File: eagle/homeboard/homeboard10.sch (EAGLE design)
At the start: 99 parts, among them IC1 XCF02S, IC2 25LC080SN, IC3 ATMEGA32U2-TQFP, Q5 BC848SMD, Q6 BC848SMD, Q7 BC848SMD, Q8 BC848SMD, T1 BSS138, T2 BC848, T3 BSS138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

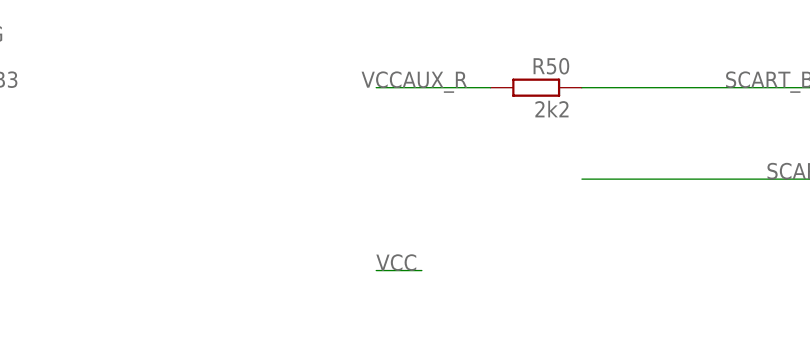
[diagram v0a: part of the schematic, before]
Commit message: reconnecting blanking pin
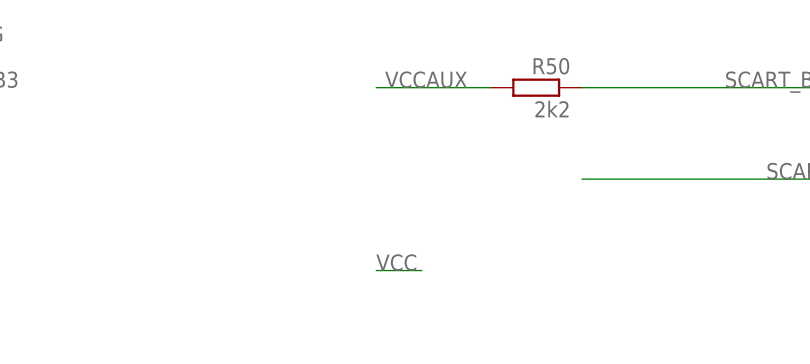
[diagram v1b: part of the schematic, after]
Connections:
- removed net VCCAUX_R: R50.2
- net VCCAUX: now also R50.2
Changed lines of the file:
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@@
 <junction x="-144.78" y="-73.66"/>
+</segment>
+<segment>
+<pinref part="R50" gate="G$1" pin="2"/>
+<wire x1="205.74" y1="276.86" x2="193.04" y2="276.86" width="0.1524" layer="91"/>
+<label x="203.2" y="276.86" size="1.778" layer="95" rot="MR0"/>
 </segment>
 </net>
@@
 </segment>
 </net>
-<net name="VCCAUX_R" class="0">
-<segment>
-<pinref part="R50" gate="G$1" pin="2"/>
-<wire x1="205.74" y1="276.86" x2="193.04" y2="276.86" width="0.1524" layer="91"/>
-<label x="203.2" y="276.86" size="1.778" layer="95" rot="MR0"/>
-</segment>
-</net>

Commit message: rework
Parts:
- added R47, R51: 270, rcl:R-EU_R0805
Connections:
- net CLK_5V: now also R47.1
- net DATA_5V: now also R51.1
- net PS2CLK: now also R47.2
- net PS2DAT: now also R51.2
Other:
- note added: "Possible alternative:"
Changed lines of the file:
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@@
 <part name="SUPPLY10" library="supply2" deviceset="GND" device=""/>
 <part name="SUPPLY11" library="supply2" deviceset="GND" device=""/>
+<part name="R47" library="rcl" deviceset="R-EU_" device="R0805" value="270"/>
+<part name="R51" library="rcl" deviceset="R-EU_" device="R0805" value="270"/>
 </parts>
 <sheets>
@@
 <plain>
 <text x="-167.64" y="86.36" size="1.778" layer="91">Choose one of these 3.3v regs</text>
+<text x="271.78" y="-254" size="1.778" layer="91">Possible alternative:</text>
 </plain>
 <instances>
@@
 <instance part="SUPPLY10" gate="GND" x="-149.86" y="50.8"/>
 <instance part="SUPPLY11" gate="GND" x="-149.86" y="27.94"/>
+<instance part="R47" gate="G$1" x="254" y="-261.62" rot="R180"/>
+<instance part="R51" gate="G$1" x="307.34" y="-261.62" rot="R180"/>
 </instances>
 <busses>
@@
 <label x="224.536" y="-196.342" size="1.778" layer="95"/>
 </segment>
+<segment>
+<wire x1="236.22" y1="-261.62" x2="248.92" y2="-261.62" width="0.1524" layer="91"/>
+<junction x="236.22" y="-261.62"/>
+<label x="232.156" y="-264.922" size="1.778" layer="95"/>
+<pinref part="R47" gate="G$1" pin="2"/>
+</segment>
 </net>
 <net name="PS2DAT" class="0">
@@
 <label x="286.004" y="-196.088" size="1.778" layer="95"/>
 </segment>
+<segment>
+<wire x1="292.1" y1="-261.62" x2="302.26" y2="-261.62" width="0.1524" layer="91"/>
+<junction x="292.1" y="-261.62"/>
+<label x="286.004" y="-264.668" size="1.778" layer="95"/>
+<pinref part="R51" gate="G$1" pin="2"/>
+</segment>
 </net>
 <net name="DATA_5V" class="0">
@@
 <label x="309.88" y="-228.6" size="1.778" layer="95"/>
 </segment>
+<segment>
+<junction x="332.74" y="-261.62"/>
+<label x="331.724" y="-264.922" size="1.778" layer="95"/>
+<pinref part="R51" gate="G$1" pin="1"/>
+<wire x1="312.42" y1="-261.62" x2="332.74" y2="-261.62" width="0.1524" layer="91"/>
+</segment>
 </net>
 <net name="CLK_5V" class="0">
@@
 <label x="309.88" y="-220.98" size="1.778" layer="95"/>
 </segment>
-</net>
+<segment>
+<wire x1="259.08" y1="-261.62" x2="269.24" y2="-261.62" width="0.1524" layer="91"/>
+<junction x="269.24" y="-261.62"/>
+<label x="268.478" y="-264.668" size="1.778" layer="95"/>
+<pinref part="R47" gate="G$1" pin="1"/>
+</segment>
+</net>

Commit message: rework
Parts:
- added C26, C27, C28, C29, C30, C31, C32: 100nF, rcl:C-EUC0603
- added R53, R54: 22, rcl:R-EU_R0805
- added X6: MINI-USB_4P-85-32004-10X, con-cypressindustries:MINI-USB_4P-85-32004-10X
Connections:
- new net N$36: R53.1, X6.2
- new net N$49: IC3.D+, R54.2
- new net N$66: R54.1, X6.3
- new net N$68: IC3.D-, R53.2
- new net N$69: IC3.UGND, X6.4
- net GND: now also C26.2, C27.2, C28.2, C29.2, C30.2, C31.2, C32.2, IC3.GND
- net VCC: now also C26.1, C27.1, C28.1, C29.1, C30.1, C31.1, C32.1, IC3.AVCC, IC3.UVCC, IC3.VCC
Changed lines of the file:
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@@
 <part name="R47" library="rcl" deviceset="R-EU_" device="R0805" value="270"/>
 <part name="R51" library="rcl" deviceset="R-EU_" device="R0805" value="270"/>
+<part name="C26" library="rcl" deviceset="C-EU" device="C0603" value="100nF"/>
+<part name="C27" library="rcl" deviceset="C-EU" device="C0603" value="100nF"/>
+<part name="C28" library="rcl" deviceset="C-EU" device="C0603" value="100nF"/>
+<part name="C29" library="rcl" deviceset="C-EU" device="C0603" value="100nF"/>
+<part name="C30" library="rcl" deviceset="C-EU" device="C0603" value="100nF"/>
+<part name="C31" library="rcl" deviceset="C-EU" device="C0603" value="100nF"/>
+<part name="C32" library="rcl" deviceset="C-EU" device="C0603" value="100nF"/>
+<part name="X6" library="con-cypressindustries" deviceset="MINI-USB_4P-" device="85-32004-10X"/>
+<part name="R53" library="rcl" deviceset="R-EU_" device="R0805" value="22"/>
+<part name="R54" library="rcl" deviceset="R-EU_" device="R0805" value="22"/>
+<part name="SUPPLY12" library="supply2" deviceset="GND" device=""/>
 </parts>
 <sheets>
@@
 <instance part="R47" gate="G$1" x="254" y="-261.62" rot="R180"/>
 <instance part="R51" gate="G$1" x="307.34" y="-261.62" rot="R180"/>
+<instance part="C26" gate="G$1" x="-147.32" y="127"/>
+<instance part="C27" gate="G$1" x="-139.7" y="127"/>
+<instance part="C28" gate="G$1" x="-132.08" y="127"/>
+<instance part="C29" gate="G$1" x="-101.6" y="127"/>
+<instance part="C30" gate="G$1" x="-124.46" y="127"/>
+<instance part="C31" gate="G$1" x="-116.84" y="127"/>
+<instance part="C32" gate="G$1" x="-109.22" y="127"/>
+<instance part="X6" gate="G$1" x="-299.72" y="-35.56" rot="MR0"/>
+<instance part="R53" gate="G$1" x="-281.94" y="-33.02" rot="MR180"/>
+<instance part="R54" gate="G$1" x="-287.02" y="-35.56" rot="MR180"/>
+<instance part="SUPPLY12" gate="GND" x="-292.1" y="-78.74"/>
 </instances>
 <busses>
@@
 <wire x1="-71.12" y1="104.14" x2="-63.5" y2="104.14" width="0.1524" layer="91"/>
 <junction x="-71.12" y="104.14"/>
+<pinref part="C26" gate="G$1" pin="2"/>
+<wire x1="-157.48" y1="121.92" x2="-147.32" y2="121.92" width="0.1524" layer="91"/>
+<pinref part="C27" gate="G$1" pin="2"/>
+<wire x1="-147.32" y1="121.92" x2="-139.7" y2="121.92" width="0.1524" layer="91"/>
+<junction x="-147.32" y="121.92"/>
+<pinref part="C28" gate="G$1" pin="2"/>
+<wire x1="-139.7" y1="121.92" x2="-132.08" y2="121.92" width="0.1524" layer="91"/>
+<junction x="-139.7" y="121.92"/>
+<pinref part="C30" gate="G$1" pin="2"/>
+<wire x1="-132.08" y1="121.92" x2="-124.46" y2="121.92" width="0.1524" layer="91"/>
+<junction x="-132.08" y="121.92"/>
+<pinref part="C31" gate="G$1" pin="2"/>
+<wire x1="-124.46" y1="121.92" x2="-116.84" y2="121.92" width="0.1524" layer="91"/>
+<junction x="-124.46" y="121.92"/>
+<pinref part="C32" gate="G$1" pin="2"/>
+<wire x1="-116.84" y1="121.92" x2="-109.22" y2="121.92" width="0.1524" layer="91"/>
+<junction x="-116.84" y="121.92"/>
+<pinref part="C29" gate="G$1" pin="2"/>
+<wire x1="-109.22" y1="121.92" x2="-101.6" y2="121.92" width="0.1524" layer="91"/>
+<junction x="-109.22" y="121.92"/>
+<wire x1="-157.48" y1="121.92" x2="-157.48" y2="104.14" width="0.1524" layer="91"/>
+<junction x="-157.48" y="104.14"/>
 </segment>
 <segment>
@@
 <junction x="-127" y="30.48"/>
 <pinref part="SUPPLY11" gate="GND" pin="GND"/>
+</segment>
+<segment>
+<pinref part="IC3" gate="G$1" pin="GND"/>
+<pinref part="SUPPLY12" gate="GND" pin="GND"/>
+<wire x1="-292.1" y1="-76.2" x2="-292.1" y2="-73.66" width="0.1524" layer="91"/>
+<wire x1="-292.1" y1="-73.66" x2="-274.32" y2="-73.66" width="0.1524" layer="91"/>
 </segment>
 </net>
@@
 </segment>
 <segment>
+<pinref part="C26" gate="G$1" pin="1"/>
+<pinref part="C27" gate="G$1" pin="1"/>
+<wire x1="-147.32" y1="129.54" x2="-139.7" y2="129.54" width="0.1524" layer="91"/>
+<junction x="-147.32" y="129.54"/>
+<pinref part="C28" gate="G$1" pin="1"/>
+<wire x1="-139.7" y1="129.54" x2="-132.08" y2="129.54" width="0.1524" layer="91"/>
+<junction x="-139.7" y="129.54"/>
+<pinref part="C30" gate="G$1" pin="1"/>
+<wire x1="-132.08" y1="129.54" x2="-124.46" y2="129.54" width="0.1524" layer="91"/>
+<junction x="-132.08" y="129.54"/>
+<pinref part="C31" gate="G$1" pin="1"/>
+<wire x1="-124.46" y1="129.54" x2="-116.84" y2="129.54" width="0.1524" layer="91"/>
+<junction x="-124.46" y="129.54"/>
+<pinref part="C32" gate="G$1" pin="1"/>
+<wire x1="-116.84" y1="129.54" x2="-109.22" y2="129.54" width="0.1524" layer="91"/>
+<junction x="-116.84" y="129.54"/>
+<pinref part="C29" gate="G$1" pin="1"/>
+<wire x1="-109.22" y1="129.54" x2="-101.6" y2="129.54" width="0.1524" layer="91"/>
+<junction x="-109.22" y="129.54"/>
 <wire x1="-167.64" y1="91.44" x2="-170.18" y2="91.44" width="0.1524" layer="91"/>
 <label x="-167.64" y="91.44" size="1.778" layer="95"/>
@@
 <wire x1="-172.72" y1="91.44" x2="-170.18" y2="91.44" width="0.1524" layer="91"/>
 <pinref part="C6" gate="G$1" pin="1"/>
-<wire x1="-170.18" y1="111.76" x2="-147.32" y2="111.76" width="0.1524" layer="91"/>
+<wire x1="-170.18" y1="111.76" x2="-165.1" y2="111.76" width="0.1524" layer="91"/>
 <junction x="-170.18" y="111.76"/>
 <pinref part="C7" gate="G$1" pin="1"/>
+<wire x1="-165.1" y1="111.76" x2="-147.32" y2="111.76" width="0.1524" layer="91"/>
 <wire x1="-147.32" y1="111.76" x2="-139.7" y2="111.76" width="0.1524" layer="91"/>
 <junction x="-147.32" y="111.76"/>
@@
 <wire x1="-71.12" y1="111.76" x2="-63.5" y2="111.76" width="0.1524" layer="91"/>
 <junction x="-71.12" y="111.76"/>
+<wire x1="-147.32" y1="129.54" x2="-165.1" y2="129.54" width="0.1524" layer="91"/>
+<wire x1="-165.1" y1="129.54" x2="-165.1" y2="111.76" width="0.1524" layer="91"/>
+<junction x="-165.1" y="111.76"/>
+</segment>
+<segment>
+<pinref part="IC3" gate="G$1" pin="AVCC"/>
+<wire x1="-274.32" y1="-25.4" x2="-279.4" y2="-25.4" width="0.1524" layer="91"/>
+<pinref part="IC3" gate="G$1" pin="UVCC"/>
+<wire x1="-274.32" y1="-22.86" x2="-279.4" y2="-22.86" width="0.1524" layer="91"/>
+<wire x1="-279.4" y1="-22.86" x2="-279.4" y2="-25.4" width="0.1524" layer="91"/>
+<junction x="-279.4" y="-25.4"/>
+<pinref part="IC3" gate="G$1" pin="VCC"/>
+<wire x1="-274.32" y1="-20.32" x2="-279.4" y2="-20.32" width="0.1524" layer="91"/>
+<wire x1="-279.4" y1="-20.32" x2="-279.4" y2="-22.86" width="0.1524" layer="91"/>
+<junction x="-279.4" y="-22.86"/>
+<wire x1="-279.4" y1="-25.4" x2="-289.56" y2="-25.4" width="0.1524" layer="91"/>
+<label x="-289.56" y="-25.4" size="1.778" layer="95"/>
 </segment>
 </net>
@@
 </segment>
 </net>
+<net name="N$36" class="0">
+<segment>
+<pinref part="X6" gate="G$1" pin="2"/>
+<wire x1="-294.64" y1="-33.02" x2="-287.02" y2="-33.02" width="0.1524" layer="91"/>
+<pinref part="R53" gate="G$1" pin="1"/>
+</segment>
+</net>
+<net name="N$66" class="0">
+<segment>
+<pinref part="R54" gate="G$1" pin="1"/>
+<pinref part="X6" gate="G$1" pin="3"/>
+<wire x1="-292.1" y1="-35.56" x2="-294.64" y2="-35.56" width="0.1524" layer="91"/>
+</segment>
+</net>
+<net name="N$68" class="0">
+<segment>
+<pinref part="IC3" gate="G$1" pin="D-"/>
+<wire x1="-276.86" y1="-33.02" x2="-274.32" y2="-33.02" width="0.1524" layer="91"/>
+<pinref part="R53" gate="G$1" pin="2"/>
+</segment>
+</net>
+<net name="N$49" class="0">
+<segment>
+<pinref part="IC3" gate="G$1" pin="D+"/>
+<wire x1="-274.32" y1="-35.56" x2="-281.94" y2="-35.56" width="0.1524" layer="91"/>
+<pinref part="R54" gate="G$1" pin="2"/>
+</segment>
+</net>
+<net name="N$69" class="0">
+<segment>
+<pinref part="X6" gate="G$1" pin="4"/>
+<wire x1="-294.64" y1="-38.1" x2="-292.1" y2="-38.1" width="0.1524" layer="91"/>
+<wire x1="-292.1" y1="-38.1" x2="-292.1" y2="-71.12" width="0.1524" layer="91"/>
+<pinref part="IC3" gate="G$1" pin="UGND"/>
+<wire x1="-292.1" y1="-71.12" x2="-274.32" y2="-71.12" width="0.1524" layer="91"/>
+</segment>
+</net>

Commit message: power socket
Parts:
- added X8: DC21MMX, powersupply:DC21MMX
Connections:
- net GND: now also X8.1, X8.3
- net VCC5: now also X8.2
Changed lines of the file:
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@@
 <clearance class="1" value="0.4"/>
+</class>
+<class number="2" name="gnd" width="0.3048" drill="0.508">
+<clearance class="2" value="0.1524"/>
 </class>
 </classes>
@@
 <part name="R54" library="rcl" deviceset="R-EU_" device="R0805" value="22"/>
 <part name="SUPPLY12" library="supply2" deviceset="GND" device=""/>
+<part name="X8" library="powersupply" deviceset="DC21MM" device="X"/>
+<part name="SUPPLY13" library="supply2" deviceset="GND" device=""/>
 </parts>
 <sheets>
@@
 <instance part="R54" gate="G$1" x="-287.02" y="-35.56" rot="MR180"/>
 <instance part="SUPPLY12" gate="GND" x="-292.1" y="-78.74"/>
+<instance part="X8" gate="G$1" x="-256.54" y="106.68"/>
+<instance part="SUPPLY13" gate="GND" x="-261.62" y="83.82"/>
 </instances>
 <busses>
@@
 <wire x1="-292.1" y1="-76.2" x2="-292.1" y2="-73.66" width="0.1524" layer="91"/>
 <wire x1="-292.1" y1="-73.66" x2="-274.32" y2="-73.66" width="0.1524" layer="91"/>
+</segment>
+<segment>
+<pinref part="X8" gate="G$1" pin="3"/>
+<wire x1="-241.3" y1="106.68" x2="-238.76" y2="106.68" width="0.1524" layer="91"/>
+<wire x1="-238.76" y1="106.68" x2="-238.76" y2="91.44" width="0.1524" layer="91"/>
+<pinref part="X8" gate="G$1" pin="1"/>
+<wire x1="-238.76" y1="91.44" x2="-261.62" y2="91.44" width="0.1524" layer="91"/>
+<wire x1="-261.62" y1="91.44" x2="-261.62" y2="96.52" width="0.1524" layer="91"/>
+<pinref part="SUPPLY13" gate="GND" pin="GND"/>
+<wire x1="-261.62" y1="86.36" x2="-261.62" y2="91.44" width="0.1524" layer="91"/>
+<junction x="-261.62" y="91.44"/>
 </segment>
 </net>
@@
 <wire x1="-208.28" y1="114.3" x2="-208.28" y2="91.44" width="0.1524" layer="91"/>
 <junction x="-208.28" y="91.44"/>
-</segment>
-</net>
+<pinref part="X8" gate="G$1" pin="2"/>
+<wire x1="-251.46" y1="96.52" x2="-226.06" y2="96.52" width="0.1524" layer="91"/>
+<wire x1="-226.06" y1="96.52" x2="-226.06" y2="73.66" width="0.1524" layer="91"/>
+<wire x1="-226.06" y1="73.66" x2="-208.28" y2="73.66" width="0.1524" layer="91"/>
+</segment>
+</net>
